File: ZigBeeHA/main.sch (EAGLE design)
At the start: 27 parts, among them IC1 REG1117, X1 5202-03-N-02

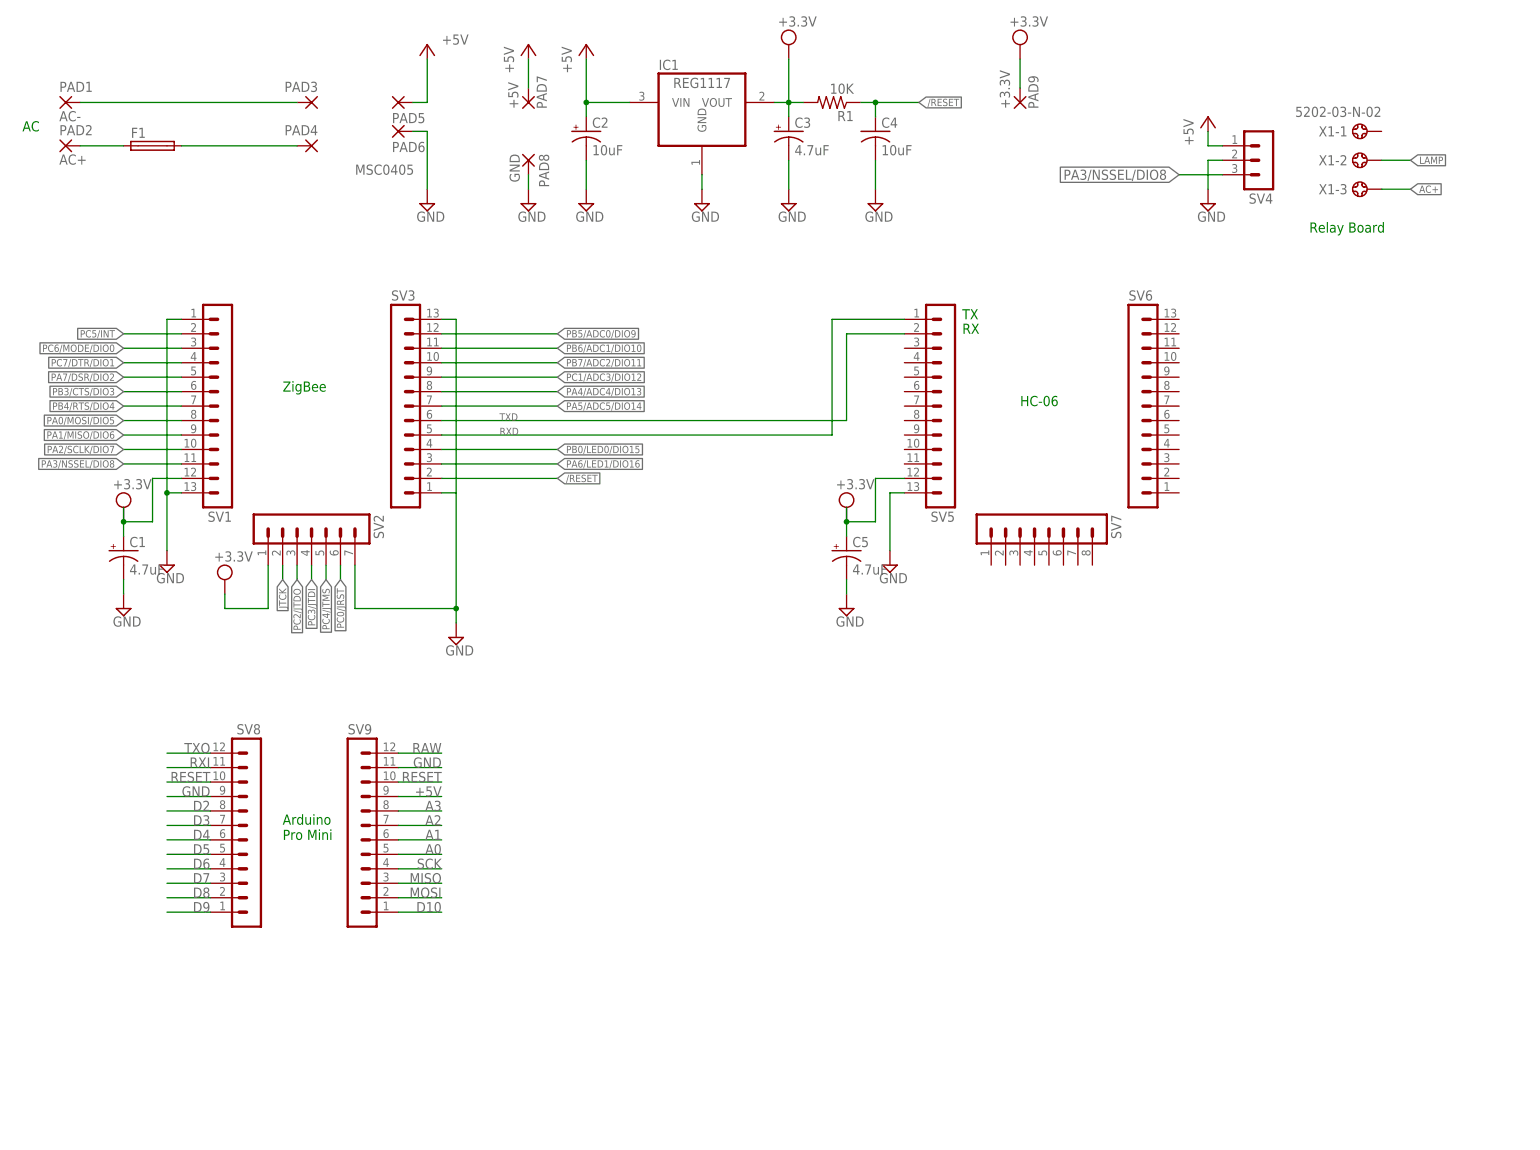
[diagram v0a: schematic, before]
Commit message: Arduino is added for Servo control
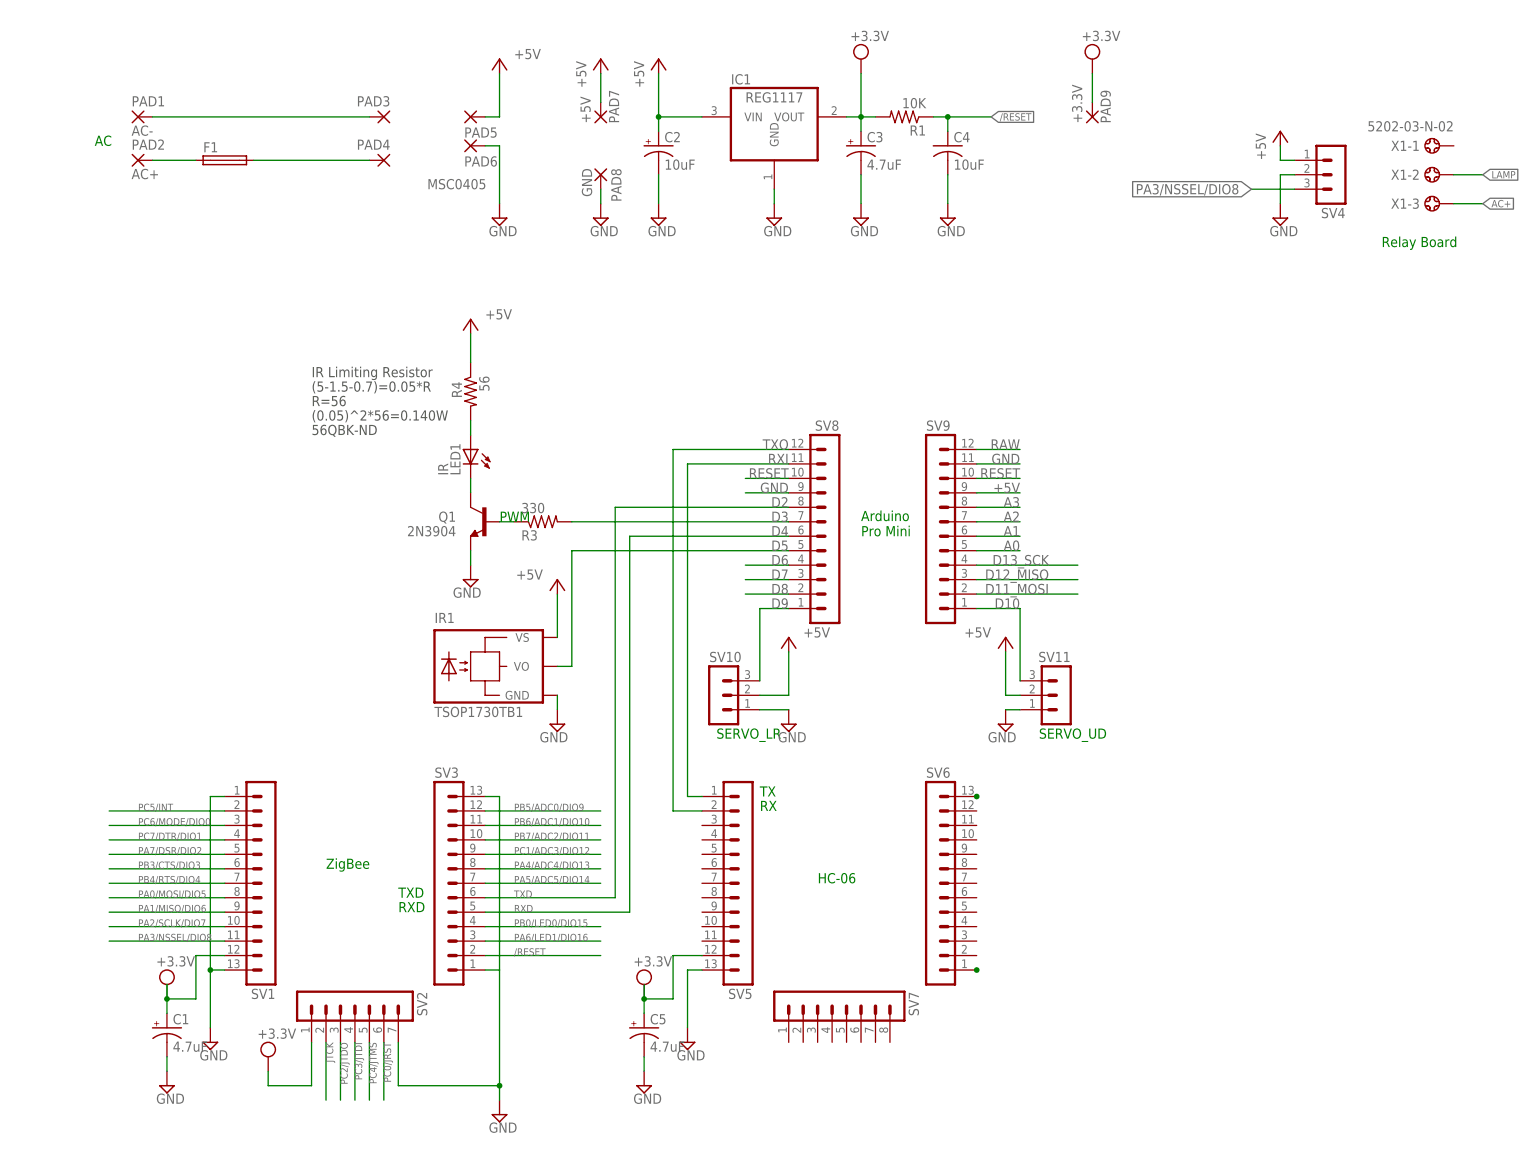
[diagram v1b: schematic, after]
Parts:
- added IR1: TSOP1730TB1, telefunken:TSOP1730TB1
- added LED1: IR, SparkFun:LED5MM
- added Q1: 2N3904, SparkFun:TRANSISTOR_NPNTO92
- added R3: 330, SparkFun:RESISTORAXIAL-0.3
- added R4: 56, SparkFun:RESISTORAXIAL-0.3
- added SV10, SV11: (no value), con-lstb:MA03-1
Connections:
- net MISO renamed D12_MISO
- net MOSI renamed D11_MOSI
- net SCK renamed D13_SCK
- new net N$5: Q1.B, R3.1
- new net N$6: LED1.A, R4.2
- new net N$7: LED1.C, Q1.C
- net +5V: now also IR1.VS, R4.1, SV10.2, SV11.2
- net D10: now also SV11.3
- net D3: now also R3.2
- net D5: now also IR1.VO
- net D9: now also SV10.3
- net GND: now also IR1.GND, Q1.E, SV10.1, SV11.1
- net RXD: no longer SV5.1
- net RXI: now also SV5.1
- net TXD: no longer SV5.2
- net TXO: now also SV5.2
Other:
- note added: "(0.05)^2*56=0.140W"
- note added: "(5-1.5-0.7)=0.05*R"
- note added: "56QBK-ND"
- note added: "IR Limiting Resistor"
- note added: "PWM"
- note added: "R=56"
- note added: "RXD"
- note added: "SERVO_LR"
- note added: "SERVO_UD"
- note added: "TXD"
- moved on the sheet: C1, C2, C3, C4, C5, F1, IC1, PAD1, PAD2, PAD3, PAD4, PAD5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

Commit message: RPi version updated
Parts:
- removed C2: 10uF, rcl:CPOL-USSANYO_SMD_A5
- removed C3: 4.7uF, rcl:CPOL-USSANYO_SMD_A5
- removed C4: 10uF, rcl:C-USC1206
- removed F1: (no value), fuse:GSH15
- removed IC1: REG1117, burr-brown:REG1117
- removed PAD1: AC-, wirepad:2,54/1,0
- removed PAD2: AC+, wirepad:2,54/1,0
- removed PAD3, PAD4, PAD5, PAD6: (no value), wirepad:2,54/0,8
- removed PAD7: +5V, wirepad:2,54/0,8
- removed PAD8: GND, wirepad:2,54/0,8
- removed PAD9: +3.3V, wirepad:2,54/0,8
- removed R1: 10K, rcl:R-US_M1206
- removed SV4: (no value), con-lstb:MA03-1
- removed X1: 5202-03-N-02, con-ebyelectro:5202-03-N-02
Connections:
- removed net AC+: X1-3.1
- removed net LAMP: X1-2.1
- removed net N$1: PAD1.P, PAD3.P
- removed net N$2: F1.1, PAD2.P
- removed net N$3: F1.2, PAD4.P
- net +5V: no longer C2.+, IC1.VIN, PAD5.P, PAD7.P, SV4.1
- net /RESET: no longer C4.1, R1.1
- net GND: no longer C2.-, C3.-, C4.2, IC1.GND, PAD6.P, PAD8.P, SV4.2
- net PA3/NSSEL/DIO8: no longer SV4.3
- net VCC: no longer C3.+, IC1.VOUT, PAD9.P, R1.2
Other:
- note removed: "AC"
- note removed: "MSC0405"
- note removed: "Relay Board"
- moved on the sheet: C1, C5, IR1, LED1, Q1, R3, R4, SV1, SV10, SV11, SV2, SV3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
